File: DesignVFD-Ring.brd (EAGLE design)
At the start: 70.1 x 70.1 mm, 34 parts, among them IC1 LMR64010XMF/NOPB, IC2 LM340S-05, U1 MAX6920AWP+, U2 LM1084IS-5.0, U3 TPS76325DBVT

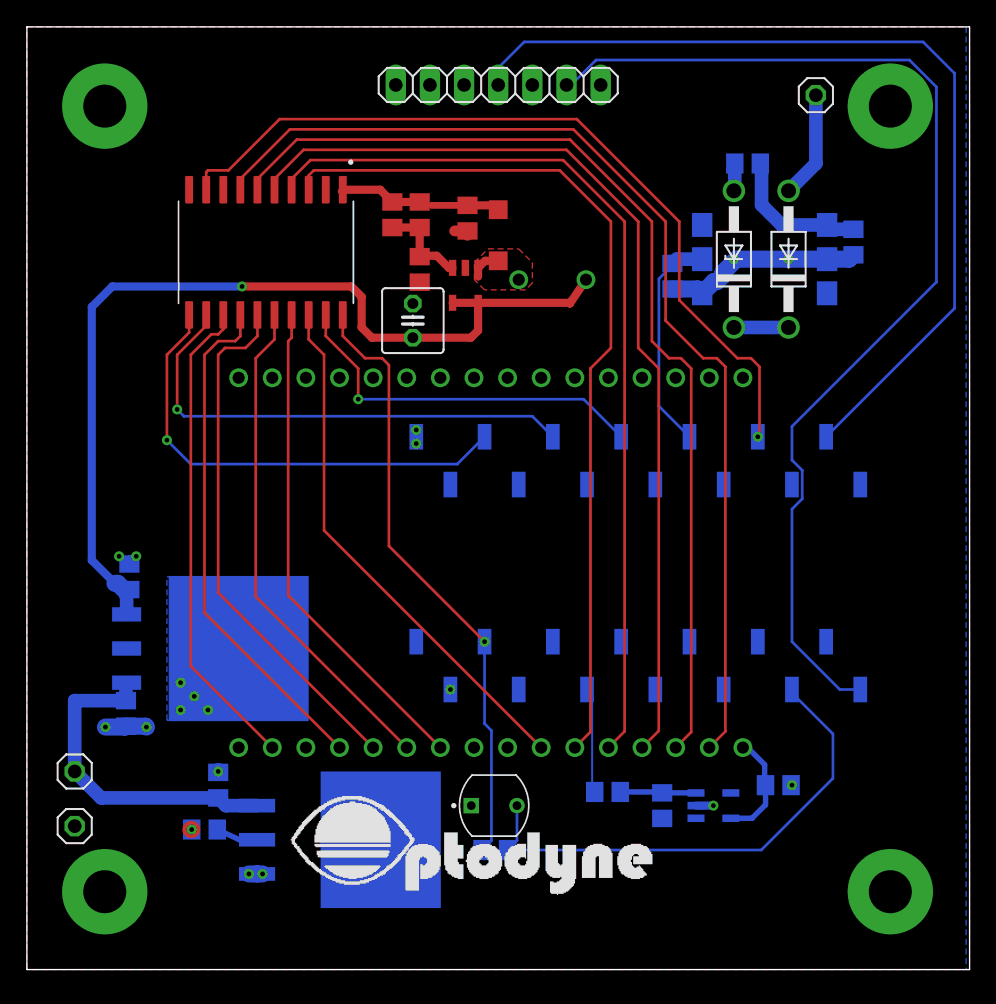
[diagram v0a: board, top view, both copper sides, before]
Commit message: changed logo, updated gerbers and created budget pic
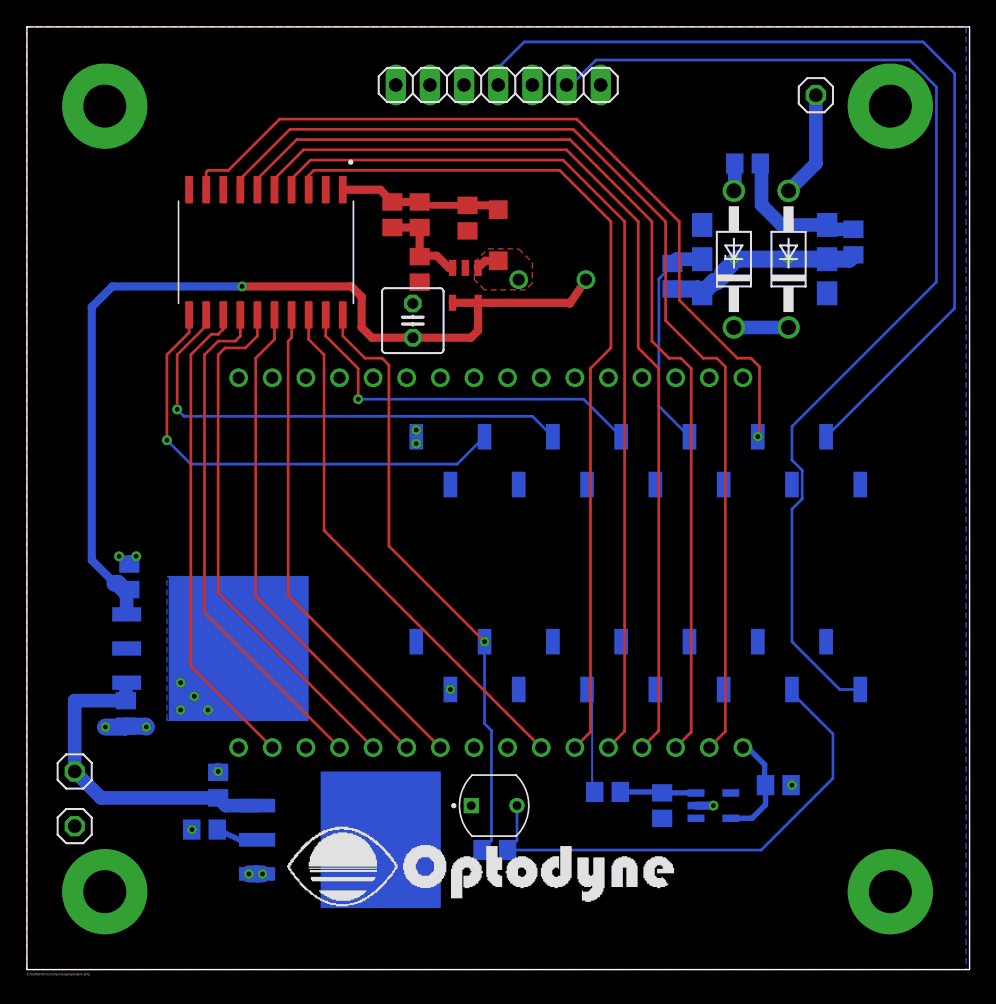
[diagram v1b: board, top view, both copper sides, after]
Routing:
- net N$6: track 2.36 -> 1.71 mm
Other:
- board text added: "E:/Git/RetroFuture-Dash/Logo/optodyne.bmp"
